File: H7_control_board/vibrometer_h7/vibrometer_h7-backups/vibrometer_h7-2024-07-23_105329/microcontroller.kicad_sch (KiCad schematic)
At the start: 34 parts, among them J2 Conn_ARM_SWD_TagConnect_TC203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, J3 Conn_01x04_Socket, Q201 BSS138, Q202 BSS138, SW201 SW_Push, U1 STM32H723VGTx, Y201 24MHz

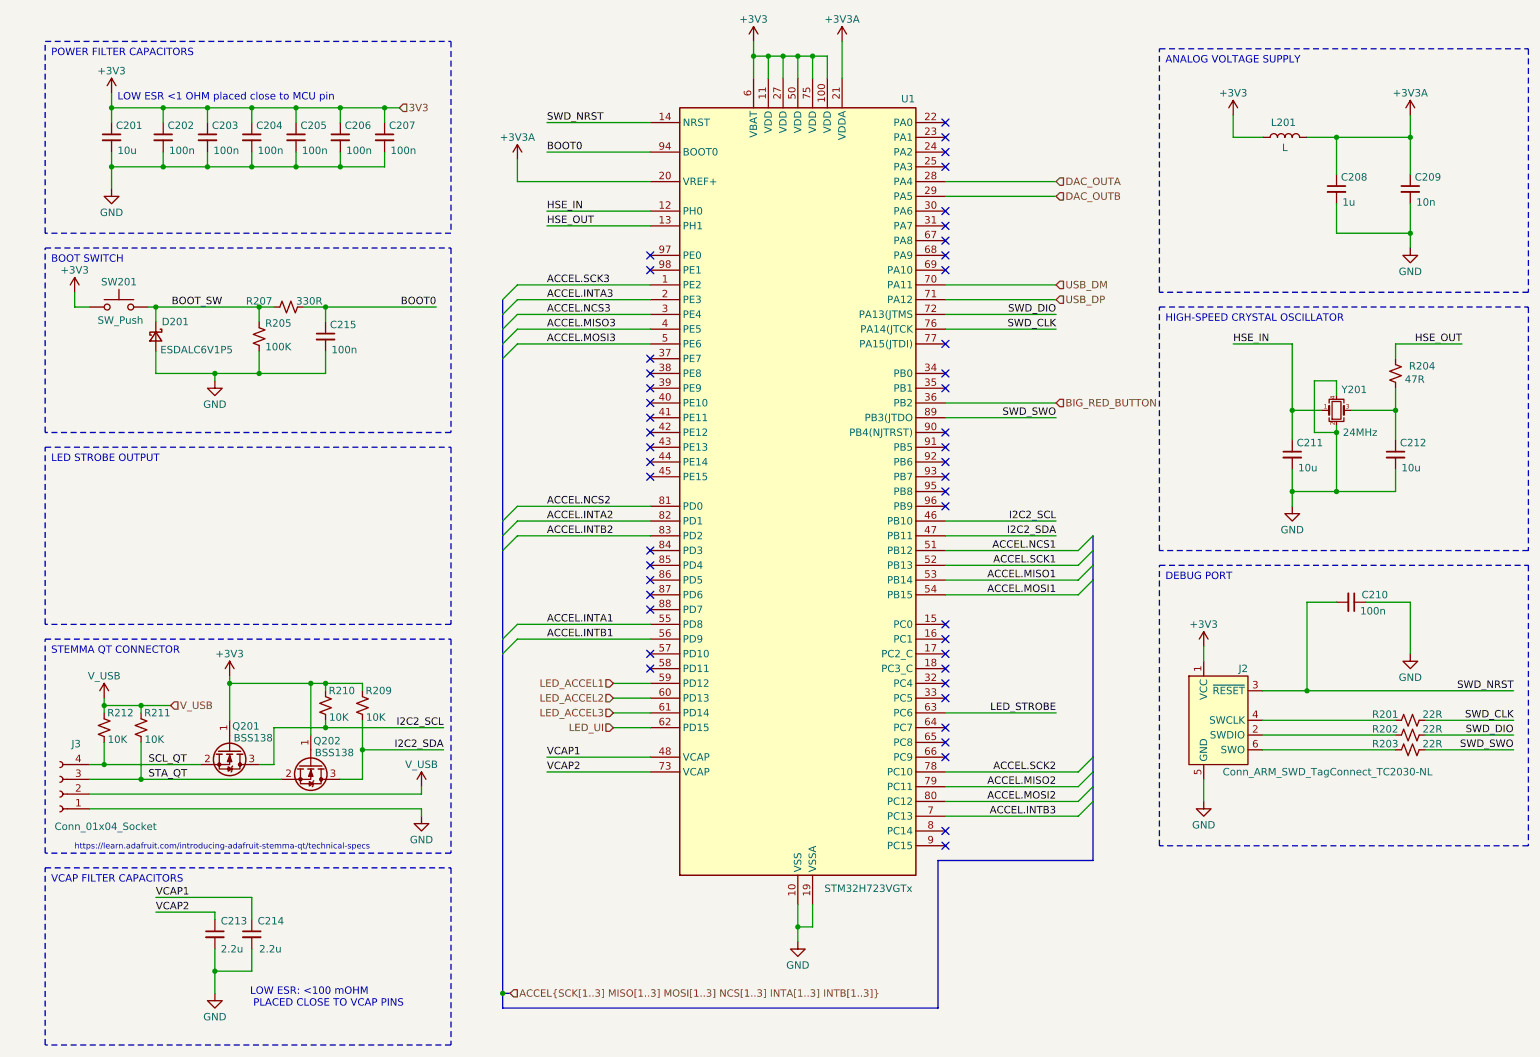
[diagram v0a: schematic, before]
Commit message: added UI leds to schematic
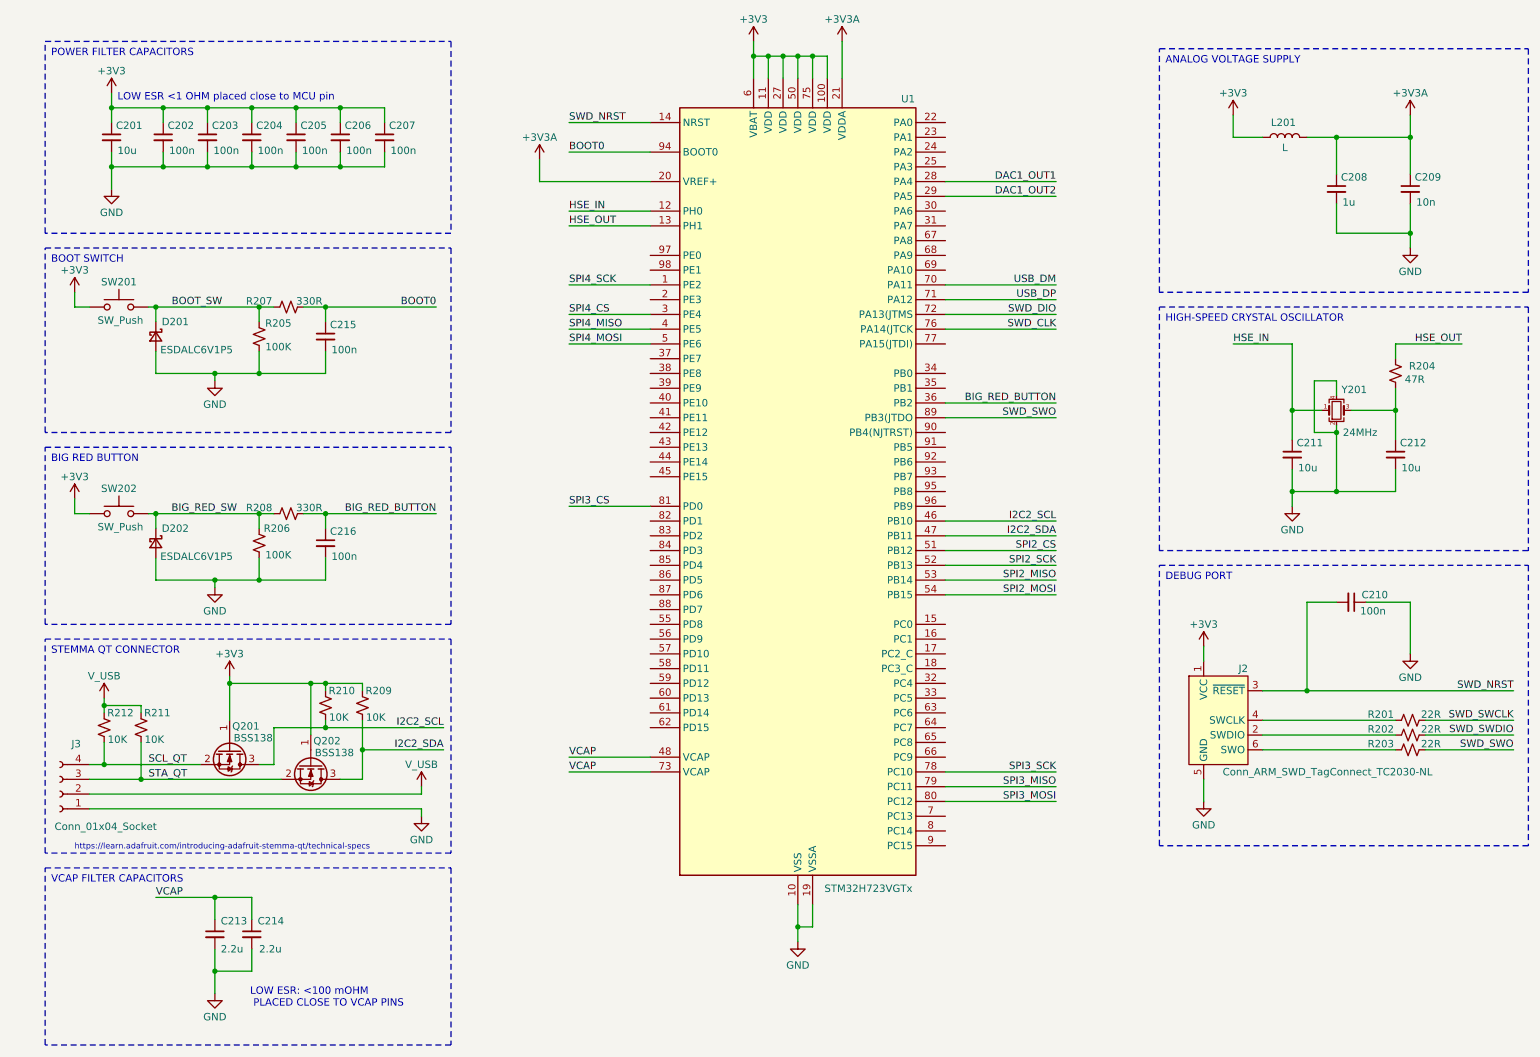
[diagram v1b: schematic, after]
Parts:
- added C216: 100n, symbol Device:C_Small
- added D202: ESDALC6V1P5, symbol Device:D_Schottky_Small
- added R206: 100K, symbol Device:R_Small_US
- added R208: 330R, symbol Device:R_Small_US
- added SW202: SW_Push, symbol Switch:SW_Push
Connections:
- net VCAP2 is gone; now on net VCAP: C213.1, U1.73 (VCAP)
- net +3V3: now also SW202.1
- net BIG_RED_BUTTON: now also C216.1, R208.2
- net GND: now also C216.2, D202.2 (A), R206.1
- net SWD_CLK: no longer R201.2
- net SWD_DIO: no longer R202.2
- net ACCEL.INTA1: no longer names the net of U1.55 (PD8)
- net ACCEL.INTA2: no longer names the net of U1.82 (PD1)
- net ACCEL.INTA3: no longer names the net of U1.2 (PE3)
- net ACCEL.INTB1: no longer names the net of U1.56 (PD9)
- net ACCEL.INTB2: no longer names the net of U1.83 (PD2)
- net ACCEL.INTB3: no longer names the net of U1.7 (PC13)
- net ACCEL.MISO1 renamed SPI2_MISO
- net ACCEL.MISO2 renamed SPI3_MISO
- net ACCEL.MISO3 renamed SPI4_MISO
- net ACCEL.MOSI1 renamed SPI2_MOSI
- net ACCEL.MOSI2 renamed SPI3_MOSI
- net ACCEL.MOSI3 renamed SPI4_MOSI
- net ACCEL.NCS1 renamed SPI2_CS
- net ACCEL.NCS2 renamed SPI3_CS
- net ACCEL.NCS3 renamed SPI4_CS
- net ACCEL.SCK1 renamed SPI2_SCK
- net ACCEL.SCK2 renamed SPI3_SCK
- net ACCEL.SCK3 renamed SPI4_SCK
- net DAC_OUTA renamed DAC1_OUT1
- net DAC_OUTB renamed DAC1_OUT2
- net LED_ACCEL1: no longer names the net of U1.59 (PD12)
- net LED_ACCEL2: no longer names the net of U1.60 (PD13)
- net LED_ACCEL3: no longer names the net of U1.61 (PD14)
- net LED_STROBE: no longer names the net of U1.63 (PC6)
- net LED_UI: no longer names the net of U1.62 (PD15)
- net VCAP1 renamed VCAP
- new net BIG_RED_SW: D202.1 (K), R206.2, R208.1, SW202.2
- new net SWD_SWCLK: R201.2
- new net SWD_SWDIO: R202.2
- no-connect marks 47 -> 0
